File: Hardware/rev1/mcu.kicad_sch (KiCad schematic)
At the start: 18 parts, among them J1 Conn_ARM_JTAG_SWD_10, SW1 SW_Push, U1 STM32F103C8Tx, U3 MS5607-02BA, U4 W25Q128JVS, Y1 16MHz

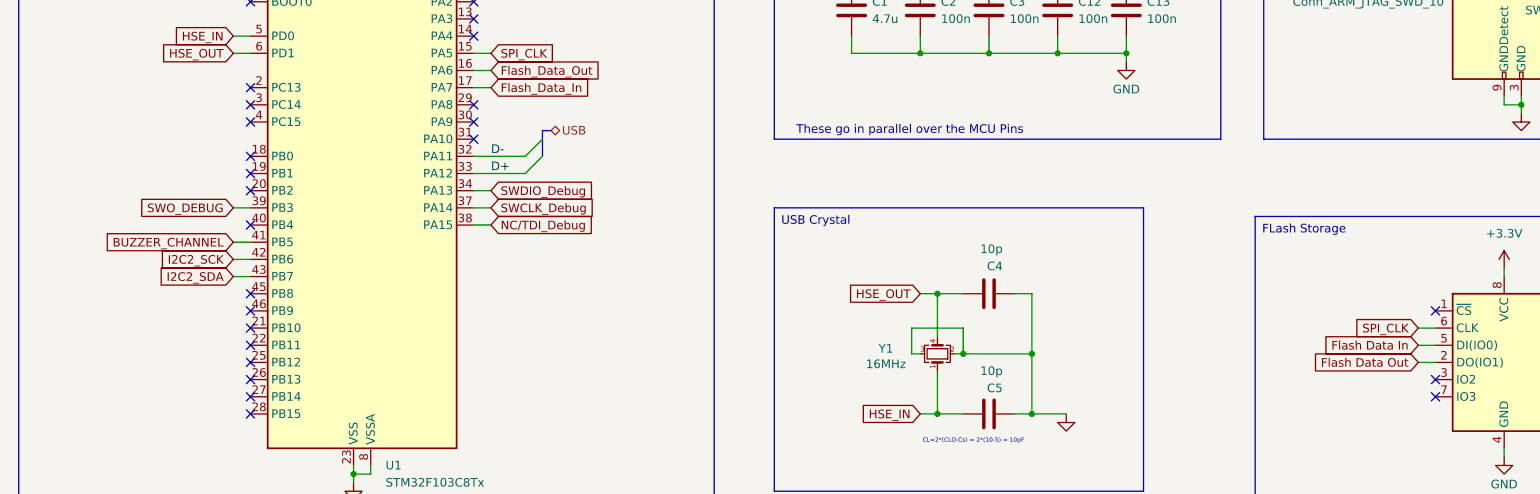
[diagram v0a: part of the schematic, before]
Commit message: Fixed the Errors
The Nets i tells ya, the nets!
need to specify the signals in the hierarchal labels
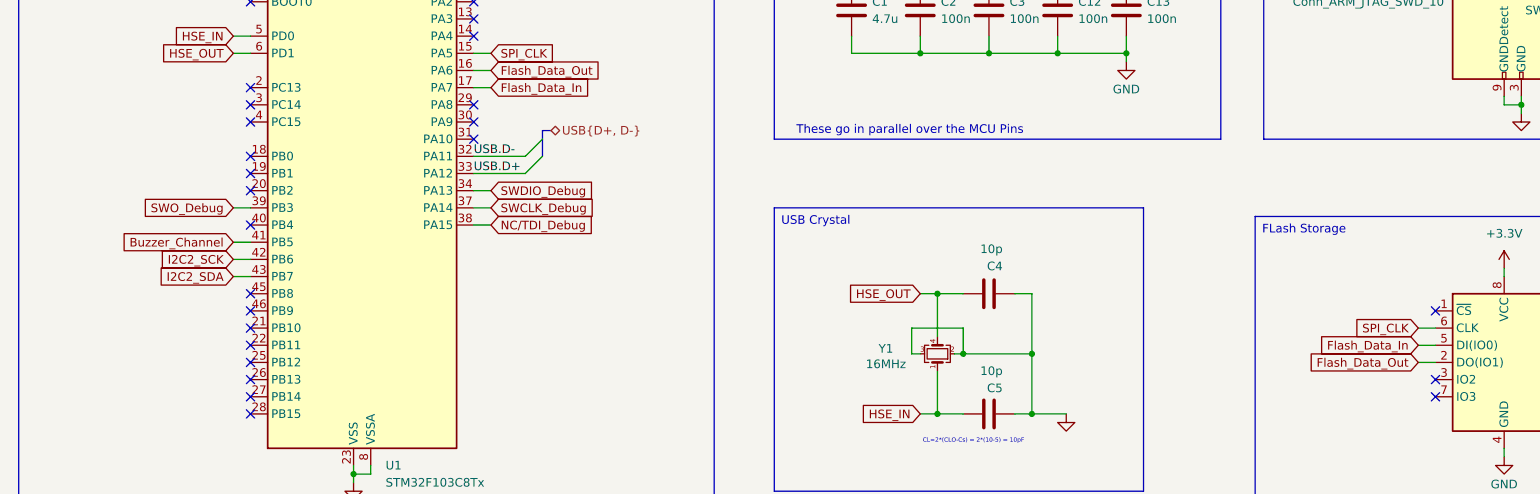
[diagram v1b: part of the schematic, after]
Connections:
- net BUZZER_CHANNEL is gone; now on net Buzzer_Channel: U1.41 (PB5)
- net Flash Data In is gone; now on net Flash_Data_In: U4.5 (DI(IO0))
- net Flash Data Out is gone; now on net Flash_Data_Out: U4.2 (DO(IO1))
- net SWO_DEBUG is gone; now on net SWO_Debug: U1.39 (PB3)
- net D+ renamed USB.D+
- net D- renamed USB.D-

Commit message: i dont know what the local change is
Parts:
- removed BZ1: Buzzer, symbol Device:Buzzer
- removed C11: 100n, symbol Device:C
- removed C6: 1u, symbol Device:C
- removed J1: Conn_ARM_JTAG_SWD_10, symbol Connector:Conn_ARM_JTAG_SWD_10
- removed R6, R7: 10k, Resistor_SMD:R_0402_1005Metric, symbol Device:R
- removed SW1: SW_Push, symbol Switch:SW_Push
- removed U3: MS5607-02BA, Package_LGA:LGA-8_3x5mm_P1.25mm, symbol Sensor_Pressure:MS5607-02BA
- removed U4: W25Q128JVS, Package_SO:SOIC-8_5.23x5.23mm_P1.27mm, symbol Memory_Flash:W25Q128JVS
- C12, C13: value 100n -> 10p; footprint (none) -> Capacitor_SMD:C_0402_1005Metric
- C4, C5: value 10p -> 100n; footprint Capacitor_SMD:C_0402_1005Metric -> (none)
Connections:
- net +3.3V: now also C4.1, C5.1; no longer C12.1, C13.1
- net HSE_IN: now also C13.1; no longer C5.1
- net HSE_OUT: now also C12.1; no longer C4.1
- net Buzzer_Channel renamed BUZZER_CHANNEL
- net Flash_Data_In renamed Flash Data In
- net Flash_Data_Out renamed Flash Data Out
- net SWO_Debug renamed SWO_DEBUG
- net USB.D+ renamed D+
- net USB.D- renamed D-
- no-connect marks 28 -> 24

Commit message: Add buses (maybe)
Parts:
- renumbered C1 to C0, C2 to C1, C3 to C2, C4 to C3, C5 to C4, C12 to C5, C13 to C6, U1 to U0
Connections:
- net BUZZER_CHANNEL renamed MCU_BUZZER
- net D+ renamed USB.D+
- net D- renamed USB.D-
- net Flash Data In renamed SPI1.MOSI
- net Flash Data Out renamed SPI1.MISO
- net NC/TDI_Debug renamed DBG.JTDI/NC
- net SPI_CLK renamed SPI1.SCLK
- net SWCLK_Debug renamed DBG.JTCK/SWCLK
- net SWDIO_Debug renamed DBG.TMS/SWDIO
- net SWO_DEBUG renamed DBG.JTDO/SWO
- net System_Reset renamed MCU_NRESET
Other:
- moved on the sheet: U0

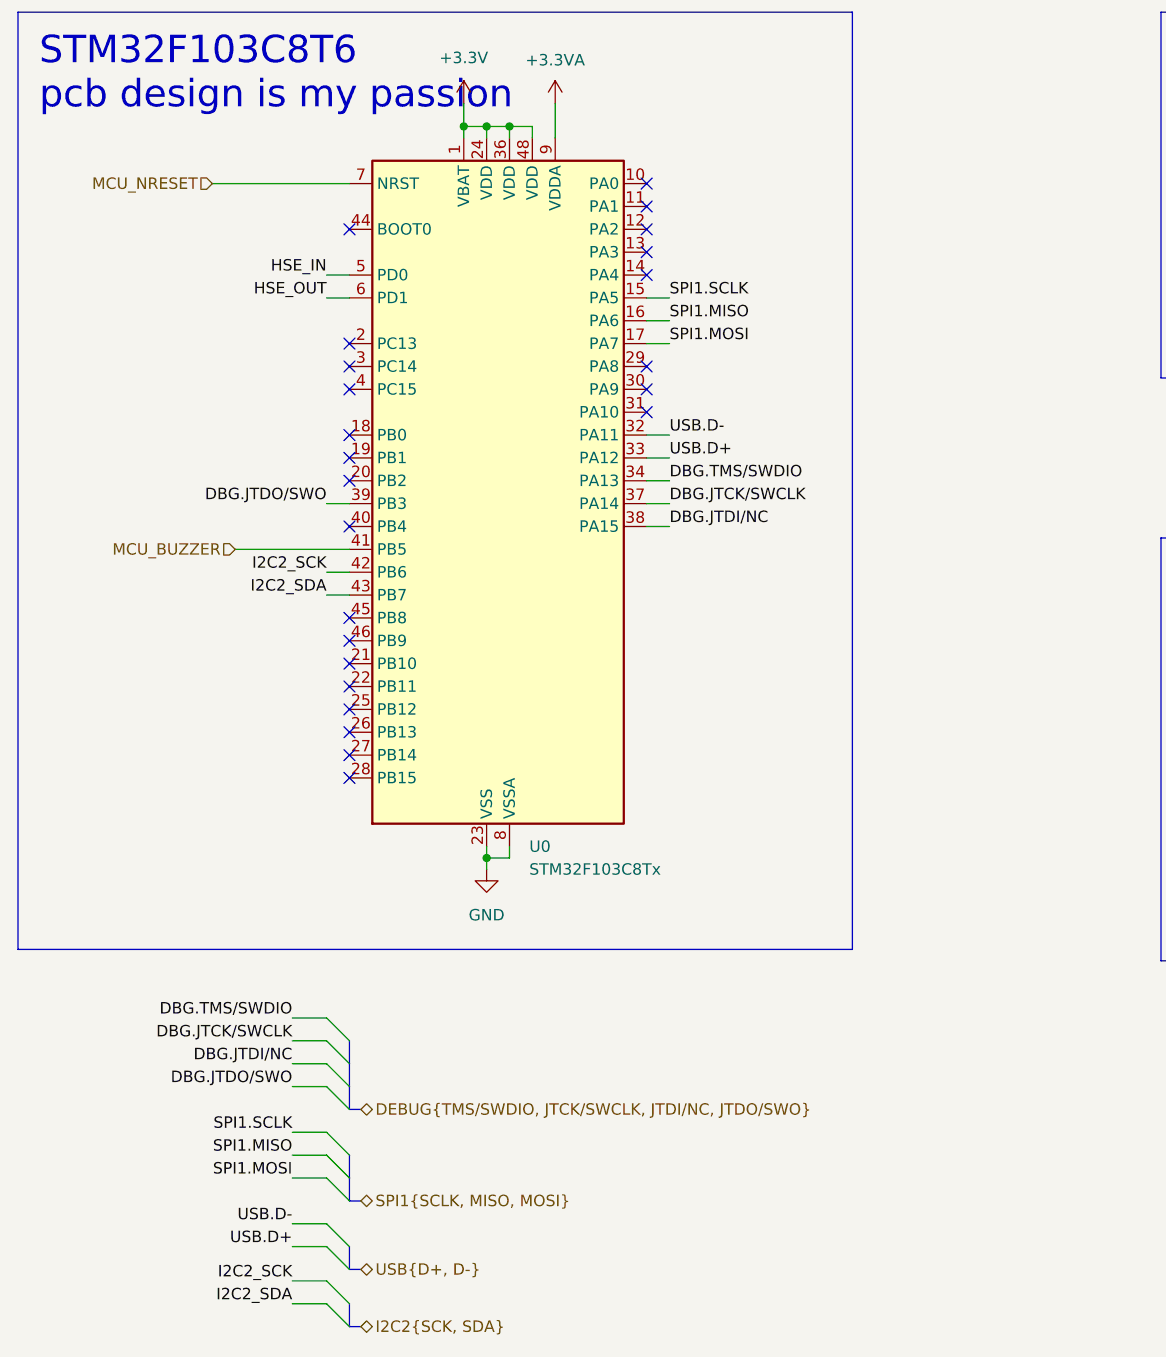
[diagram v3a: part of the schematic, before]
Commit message: Removed backup files and folder as redundant on GitHub, updated hierarchical labels to include NRESET
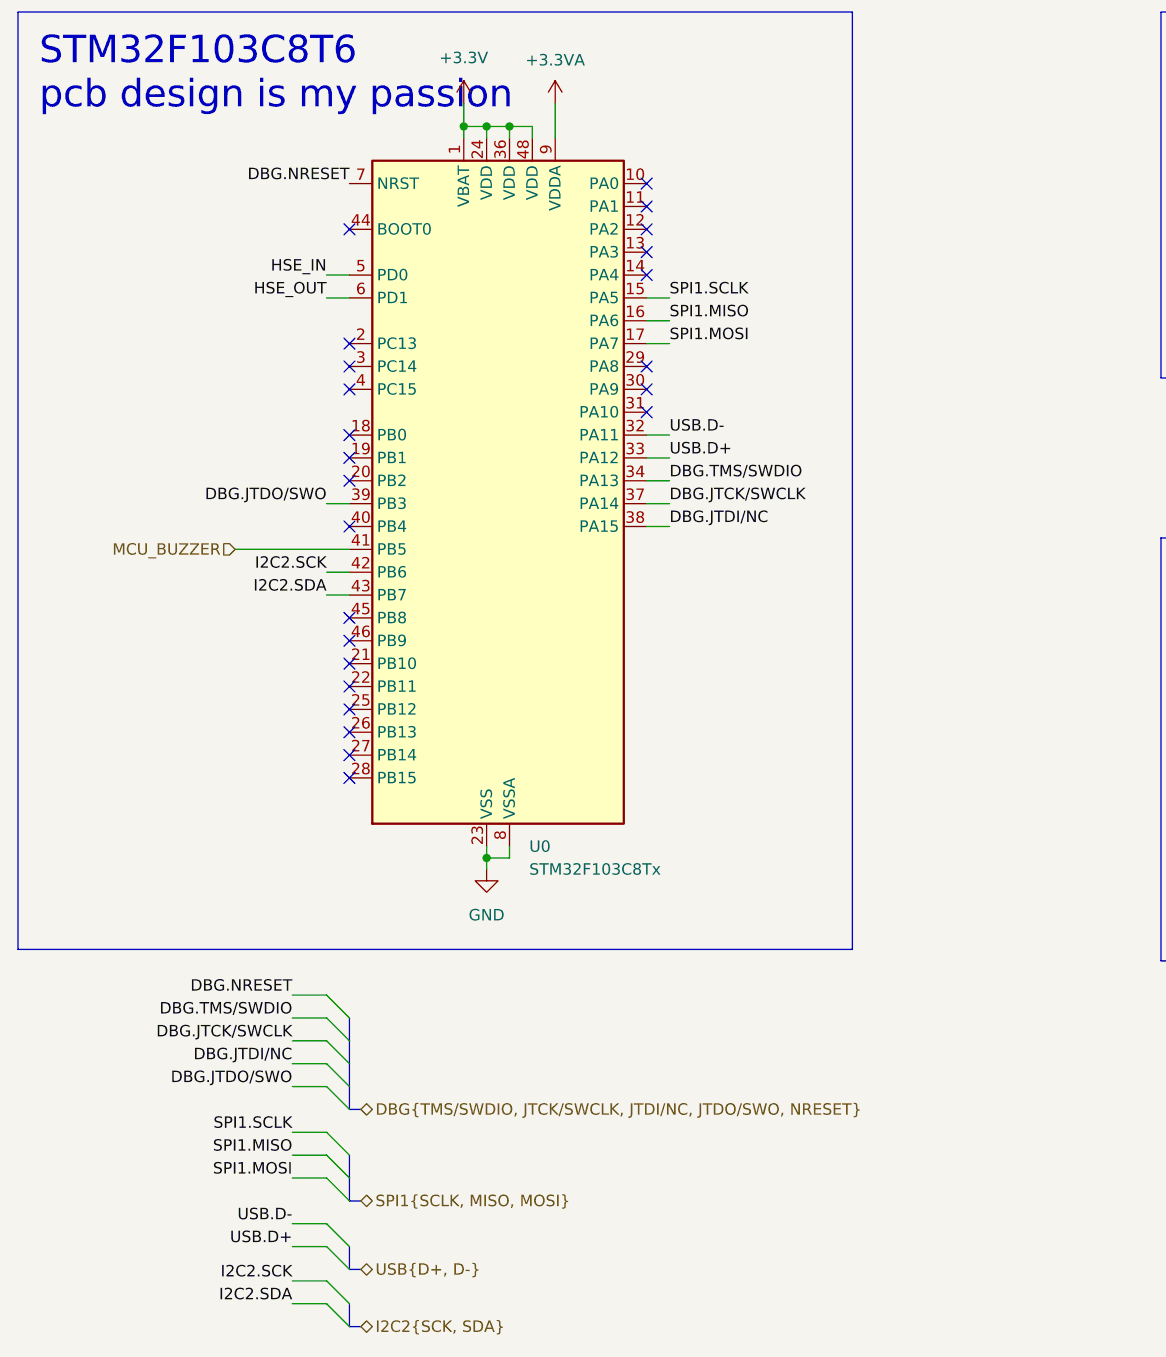
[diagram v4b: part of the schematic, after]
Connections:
- net I2C2_SCK renamed I2C2.SCK
- net I2C2_SDA renamed I2C2.SDA
- net MCU_NRESET renamed DBG.NRESET
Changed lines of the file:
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@@
+	)
+	(bus_entry
+		(at 80.01 143.51)
+		(size 2.54 2.54)
+		(stroke
+			(width 0)
+			(type default)
+		)
 	)
 	(bus_entry
@@
 	(wire
 		(pts
+			(xy 76.2 143.51) (xy 80.01 143.51)
+		)
+		(stroke
+			(width 0)
+			(type default)
+		)
+	)
+	(wire
+		(pts
 			(xy 115.57 68.58) (xy 118.11 68.58)
 		)
@@
 	(wire
 		(pts
-			(xy 67.31 53.34) (xy 82.55 53.34)
-		)
-		(stroke
-			(width 0)
-			(type default)
-		)
-	)
-	(wire
-		(pts
 			(xy 95.25 46.99) (xy 97.79 46.99)
 		)
@@
 		(pts
 			(xy 76.2 158.75) (xy 80.01 158.75)
+		)
+		(stroke
+			(width 0)
+			(type default)
+		)
+	)
+	(bus
+		(pts
+			(xy 82.55 146.05) (xy 82.55 148.59)
 		)
 		(stroke
@@
 		)
 	)
+	(label "DBG.NRESET"
+		(at 76.2 143.51 180)
+		(fields_autoplaced yes)
+		(effects
+			(font
+				(size 1.27 1.27)
+			)
+			(justify right bottom)
+		)
+	)
 	(label "SPI1.SCLK"
 		(at 118.11 66.04 0)
@@
 		)
 	)
-	(label "I2C2_SCK"
+	(label "I2C2.SCK"
 		(at 80.01 96.52 180)
 		(fields_autoplaced yes)
@@
 		)
 	)
-	(label "I2C2_SDA"
+	(label "I2C2.SDA"
 		(at 76.2 177.8 180)
 		(fields_autoplaced yes)
@@
 		)
 	)
-	(label "I2C2_SDA"
+	(label "I2C2.SDA"
 		(at 80.01 99.06 180)
 		(fields_autoplaced yes)
@@
 		)
 	)
-	(label "I2C2_SCK"
+	(label "DBG.NRESET"
+		(at 82.55 53.34 180)
+		(fields_autoplaced yes)
+		(effects
+			(font
+				(size 1.27 1.27)
+			)
+			(justify right bottom)
+		)
+	)
+	(label "I2C2.SCK"
 		(at 76.2 175.26 180)
 		(fields_autoplaced yes)
@@
 		)
 	)
-	(hierarchical_label "DEBUG{TMS{slash}SWDIO, JTCK{slash}SWCLK, JTDI{slash}NC, JTDO{slash}SWO}"
+	(hierarchical_label "DBG{TMS{slash}SWDIO, JTCK{slash}SWCLK, JTDI{slash}NC, JTDO{slash}SWO, NRESET}"
 		(shape bidirectional)
 		(at 83.82 156.21 0)
@@
 		)
 	)
-	(hierarchical_label "MCU_NRESET"
-		(shape input)
-		(at 67.31 53.34 180)
-		(fields_autoplaced yes)
-		(effects
-			(font
-				(size 1.27 1.27)
-			)
-			(justify right)
-		)
-	)

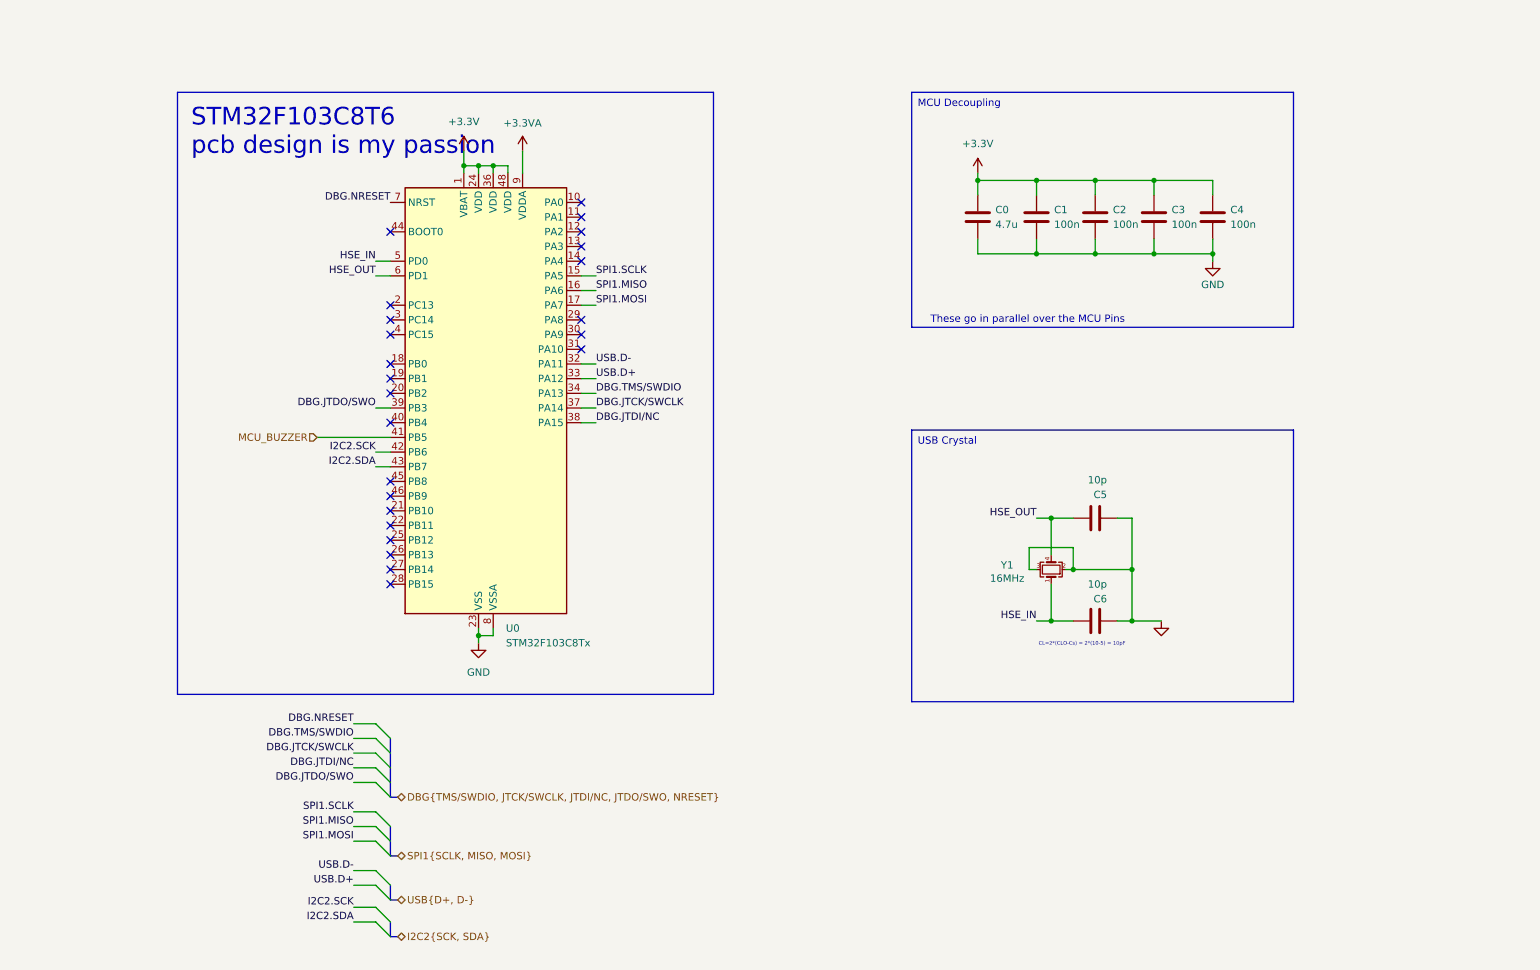
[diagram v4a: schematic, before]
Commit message: Finish schematics, assign footprints
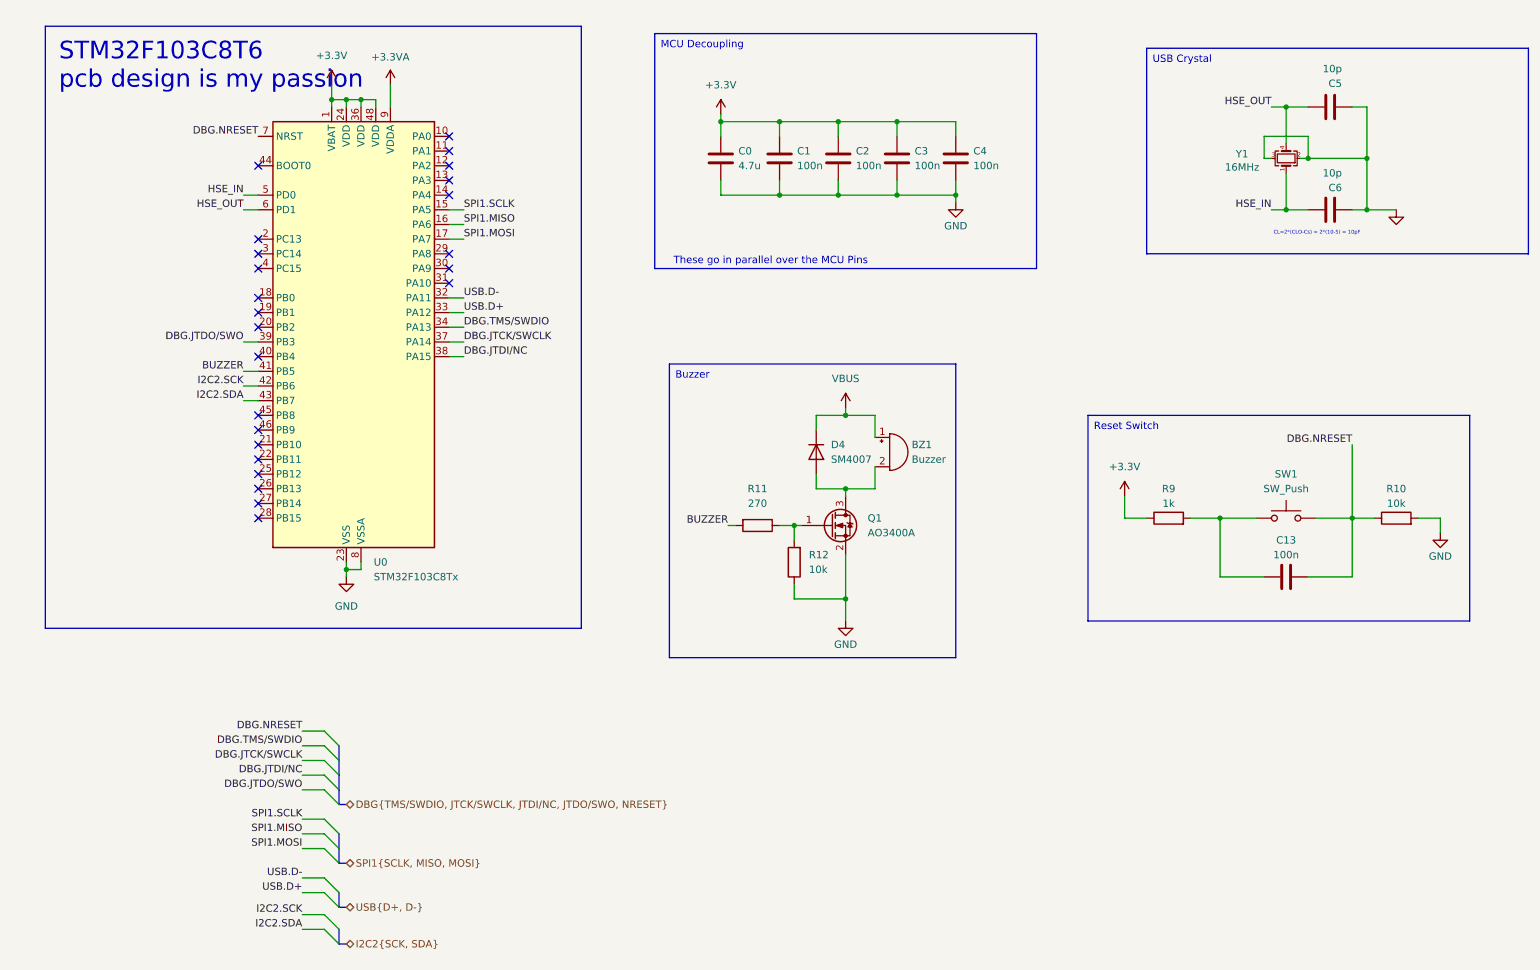
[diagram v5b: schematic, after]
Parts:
- added BZ1: Buzzer, Buzzer_Beeper:MagneticBuzzer_Kingstate_KCG0601, symbol Device:Buzzer
- added C13: 100n, Capacitor_SMD:C_0402_1005Metric, symbol Device:C
- added D4: SM4007, Diode_SMD:D_SOD-123F, symbol Diode:SM4007
- added Q1: AO3400A, Package_TO_SOT_SMD:SOT-23, symbol Transistor_FET:AO3400A
- added R10, R12: 10k, Resistor_SMD:R_0603_1608Metric, symbol Device:R
- added R11: 270, Resistor_SMD:R_0603_1608Metric, symbol Device:R
- added R9: 1k, Resistor_SMD:R_0603_1608Metric, symbol Device:R
- added SW1: SW_Push, Button_Switch_SMD:SW_Push_1P1T_XKB_TS-1187A, symbol Switch:SW_Push
- C0: footprint (none) -> Buzzer_Beeper:MagneticBuzzer_Kingstate_KCG0601
- C1, C2, C3, C4: footprint (none) -> Capacitor_SMD:C_0402_1005Metric
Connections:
- net +3.3V: now also R9.1
- net DBG.NRESET: now also C13.2, R10.1, SW1.2
- net GND: now also Q1.2 (S), R10.2, R12.1
- net MCU_BUZZER renamed BUZZER
- net BUZZER: now also R11.2
- new net: BZ1.2 (-), D4.2 (A), Q1.3 (D)
- new net: Q1.1 (G), R11.1, R12.2
- new net: C13.1, R9.2, SW1.1
- new net VBUS: BZ1.1 (+), D4.1 (K)
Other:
- moved on the sheet: C0, C1, C2, C3, C4, C5, C6, U0, Y1

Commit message: Revert "Merge remote-tracking branch 'origin/dev'"
This reverts commit 9d6b38d1428df59ab2602e839e1db75647d3fbc2, reversing
changes made to aa461fd2fa90bcdcb689545e3dbed326723346fe.
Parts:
- removed BZ1: Buzzer, Buzzer_Beeper:MagneticBuzzer_Kingstate_KCG0601, symbol Device:Buzzer
- removed C13: 100n, Capacitor_SMD:C_0402_1005Metric, symbol Device:C
- removed D4: SM4007, Diode_SMD:D_SOD-123F, symbol Diode:SM4007
- removed Q1: AO3400A, Package_TO_SOT_SMD:SOT-23, symbol Transistor_FET:AO3400A
- removed R10, R12: 10k, Resistor_SMD:R_0603_1608Metric, symbol Device:R
- removed R11: 270, Resistor_SMD:R_0603_1608Metric, symbol Device:R
- removed R9: 1k, Resistor_SMD:R_0603_1608Metric, symbol Device:R
- removed SW1: SW_Push, Button_Switch_SMD:SW_Push_1P1T_XKB_TS-1187A, symbol Switch:SW_Push
- C0: footprint Buzzer_Beeper:MagneticBuzzer_Kingstate_KCG0601 -> (none)
- C1, C2, C3, C4: footprint Capacitor_SMD:C_0402_1005Metric -> (none)
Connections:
- net BUZZER renamed MCU_BUZZER
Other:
- moved on the sheet: C0, C1, C2, C3, C4, C5, C6, U0, Y1
